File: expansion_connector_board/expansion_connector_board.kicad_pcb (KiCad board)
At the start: 2 copper layers, 139 x 89 mm, 13 parts, among them J1 Conn_01x04, J12 Conn_02x17_Top_Bottom, J13 Conn_01x04, J14 Conn_02x17_Top_Bottom, J2 ESP32 JTAG+UART (TE0790), J3 ESP32 UART Breakout, J4 ESP32 Bootstraps, J5 ESP32 Sensor, J6 ESP32/Peripheral UART Interfa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, U1 ESP32-WROOM-32D

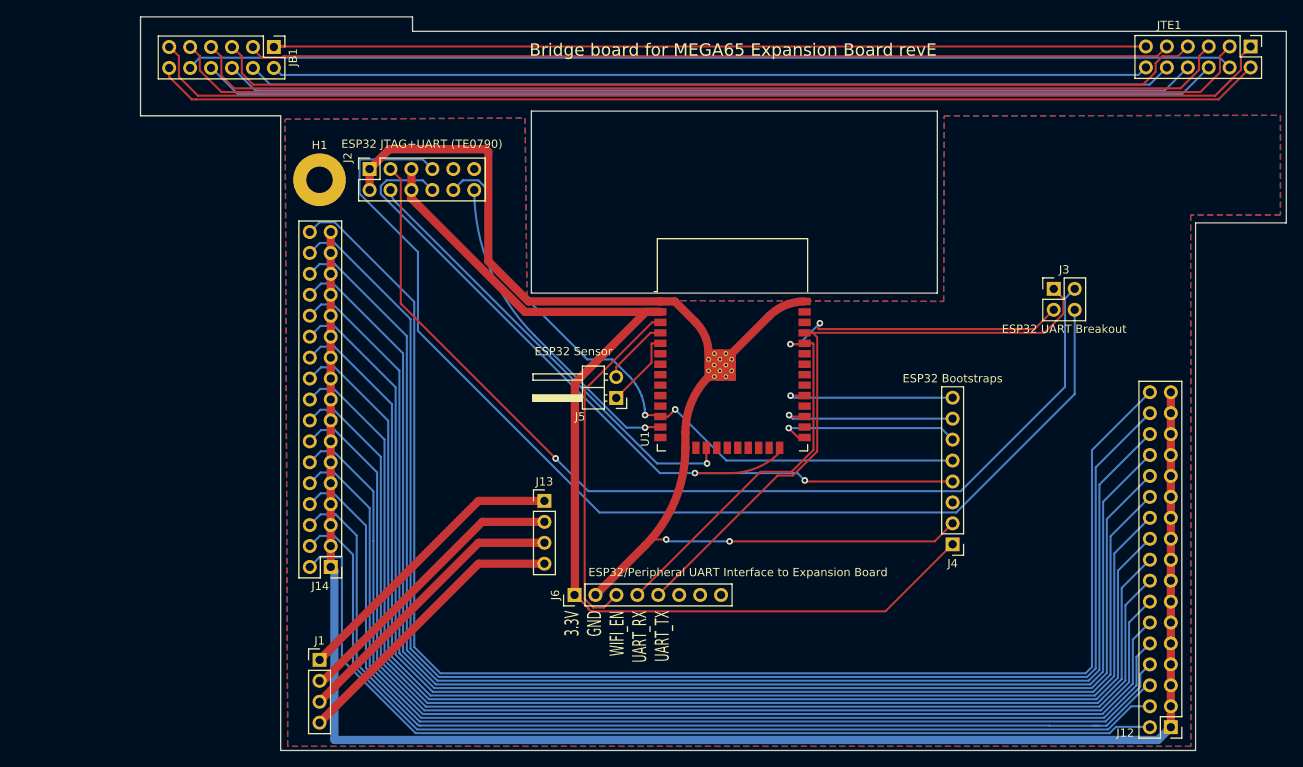
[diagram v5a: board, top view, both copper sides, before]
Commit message: add MEGA65 and open hardware logos etc
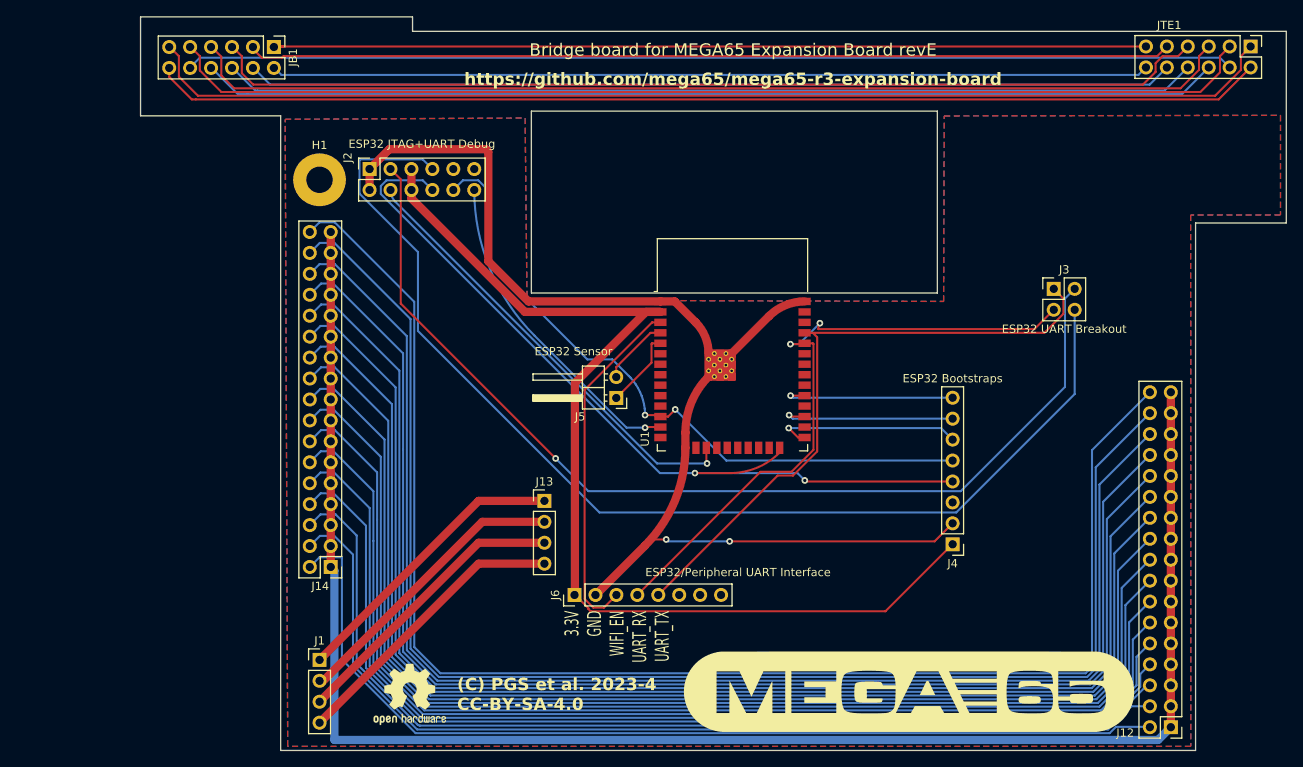
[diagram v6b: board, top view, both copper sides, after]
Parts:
- added G1: LOGO, 00Project:MEGA65-logo, F.Cu at (150.2, 116.9)
- added SYM1: Logo_Open_Hardware_Small, Symbol:OSHW-Logo2_9.8x8mm_SilkScreen, F.Cu at (89.7, 117.2)
- J2: value ESP32 JTAG+UART (TE0790) -> ESP32 JTAG+UART Debug
- J6: value ESP32/Peripheral UART Interface to Expansion Board -> ESP32/Peripheral UART Interface
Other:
- board text added: "(C) PGS et al. 2023-4 CC-BY-SA-4.0"
- board text added: "https://github.com/mega65/mega65-r3-expansion-board"

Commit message: add audio J19 pickup header
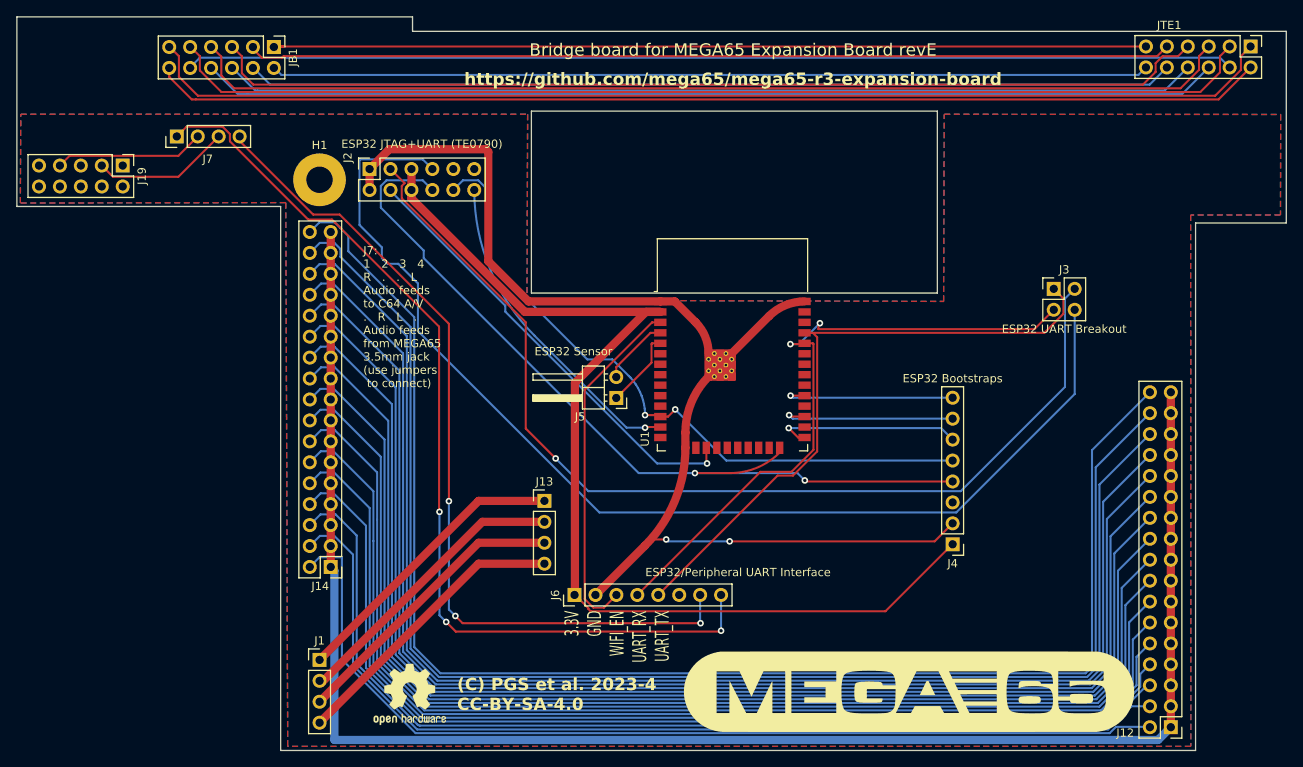
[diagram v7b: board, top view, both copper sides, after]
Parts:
- added J19: MEGA65 R4+ Analog Audio Header, Connector_PinHeader_2.54mm:PinHeader_2x05_P2.54mm_Vertical, F.Cu at (54.8, 53.0)
- added J7: Conn_01x04, Connector_PinHeader_2.54mm:PinHeader_1x04_P2.54mm_Vertical, F.Cu at (61.4, 49.5)
- J2: value ESP32 JTAG+UART Debug -> ESP32 JTAG+UART (TE0790)
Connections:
- J6 pad 7: unconnected-(J6-Pin_7-Pad7) -> AUDIO_L
- J6 pad 8: unconnected-(J6-Pin_8-Pad8) -> AUDIO_R
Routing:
- net AUDIO_R: track 0.00 -> 117.3 mm, vias 0 -> 3
- net AUDIO_L: track 0.00 -> 104.5 mm, vias 0 -> 3
- net Net-(J19-Pin_7): track 0.00 -> 18.2 mm
- net Net-(J19-Pin_3): track 0.00 -> 16.8 mm
- net JTAG_MTDO: track 103.3 -> 104.8 mm
- net /TE0790_B: track 138.0 -> 138.8 mm
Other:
- board size 139 x 89 mm -> 154 x 89 mm
- board text added: "J7: 1 2 3 4 R . . L Audio feeds to C64 A/V . R L . Audio feeds from MEGA65 3.5mm jack (use jumpers to connect)"

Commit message: gerbers exported and uploaded to pcbway
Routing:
- net AUDIO_L: track 104.5 -> 108.1 mm
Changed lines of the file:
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@@
   )
   (dimension (type aligned) (layer "Cmts.User")
-    (pts (xy 57 35) (xy 196.01 35))
+    (pts (xy 42 35) (xy 196.01 35))
     (height -1.913458)
-    (gr_text "139.0100 mm" (at 126.505 31.936542) (layer "Cmts.User")
+    (gr_text "154.0100 mm" (at 119.005 31.936542) (layer "Cmts.User")
       (effects (font (size 1 1) (thickness 0.15)))
     )
@@
   (segment (start 136.1186 81.2038) (end 155.5242 81.2038) (width 0.25) (layer "B.Cu") (net 74))
   (segment (start 135.8646 80.9498) (end 136.1186 81.2038) (width 0.25) (layer "B.Cu") (net 74))
-  (segment (start 69.0218 50.054703) (end 77.945897 58.9788) (width 0.25) (layer "F.Cu") (net 76))
+  (segment (start 70.7546 51.2374) (end 80.174703 51.2374) (width 0.25) (layer "F.Cu") (net 76))
   (segment (start 124.9426 108.5596) (end 96.0766 108.5596) (width 0.25) (layer "F.Cu") (net 76))
+  (segment (start 94.4118 72.2376) (end 94.4118 93.7514) (width 0.25) (layer "F.Cu") (net 76))
+  (segment (start 69.0218 49.5046) (end 70.7546 51.2374) (width 0.25) (layer "F.Cu") (net 76))
   (segment (start 96.0766 108.5596) (end 95.1992 107.6822) (width 0.25) (layer "F.Cu") (net 76))
-  (segment (start 69.0218 49.5046) (end 69.0218 50.054703) (width 0.25) (layer "F.Cu") (net 76))
-  (segment (start 81.153 58.9788) (end 81.9404 59.7662) (width 0.25) (layer "F.Cu") (net 76))
-  (segment (start 81.9404 59.7662) (end 94.4118 72.2376) (width 0.25) (layer "F.Cu") (net 76))
-  (segment (start 94.4118 72.2376) (end 94.4118 93.7514) (width 0.25) (layer "F.Cu") (net 76))
-  (segment (start 77.945897 58.9788) (end 81.153 58.9788) (width 0.25) (layer "F.Cu") (net 76))
+  (segment (start 80.174703 51.2374) (end 82.2396 53.302297) (width 0.25) (layer "F.Cu") (net 76))
+  (segment (start 82.2396 60.0654) (end 94.4118 72.2376) (width 0.25) (layer "F.Cu") (net 76))
+  (segment (start 82.2396 53.302297) (end 82.2396 60.0654) (width 0.25) (layer "F.Cu") (net 76))
   (via (at 124.9426 108.5596) (size 0.8) (drill 0.4) (layers "F.Cu" "B.Cu") (net 76))
   (via (at 94.4118 93.7514) (size 0.8) (drill 0.4) (layers "F.Cu" "B.Cu") (net 76))
@@
   (segment (start 124.8918 105.1306) (end 124.8918 108.5088) (width 0.25) (layer "B.Cu") (net 76))
   (segment (start 94.4118 106.8948) (end 95.1992 107.6822) (width 0.25) (layer "B.Cu") (net 76))
-  (segment (start 67.8468 50.0922) (end 77.343 59.5884) (width 0.25) (layer "F.Cu") (net 77))
   (segment (start 95.25 109.5756) (end 94.0816 108.4072) (width 0.25) (layer "F.Cu") (net 77))
+  (segment (start 61.4018 49.5046) (end 62.5768 48.3296) (width 0.25) (layer "F.Cu") (net 77))
+  (segment (start 70.7247 51.6874) (end 75.1896 56.1523) (width 0.25) (layer "F.Cu") (net 77))
+  (segment (start 93.218 94.996) (end 93.2688 95.0468) (width 0.25) (layer "F.Cu") (net 77))
+  (segment (start 78.555497 59.5884) (end 80.230101 59.5884) (width 0.25) (layer "F.Cu") (net 77))
+  (segment (start 127.3302 109.5756) (end 95.25 109.5756) (width 0.25) (layer "F.Cu") (net 77))
+  (segment (start 66.968501 48.3296) (end 67.8468 49.207899) (width 0.25) (layer "F.Cu") (net 77))
+  (segment (start 127.4318 109.474) (end 127.3302 109.5756) (width 0.25) (layer "F.Cu") (net 77))
+  (segment (start 62.5768 48.3296) (end 66.968501 48.3296) (width 0.25) (layer "F.Cu") (net 77))
+  (segment (start 67.8468 49.207899) (end 67.8468 49.991301) (width 0.25) (layer "F.Cu") (net 77))
   (segment (start 93.218 72.576299) (end 93.218 94.996) (width 0.25) (layer "F.Cu") (net 77))
-  (segment (start 62.5768 48.3296) (end 66.968501 48.3296) (width 0.25) (layer "F.Cu") (net 77))
+  (segment (start 75.1896 56.1523) (end 75.1896 56.222503) (width 0.25) (layer "F.Cu") (net 77))
+  (segment (start 69.542899 51.6874) (end 70.7247 51.6874) (width 0.25) (layer "F.Cu") (net 77))
   (segment (start 80.230101 59.5884) (end 93.218 72.576299) (width 0.25) (layer "F.Cu") (net 77))
-  (segment (start 127.3302 109.5756) (end 95.25 109.5756) (width 0.25) (layer "F.Cu") (net 77))
-  (segment (start 127.4318 109.474) (end 127.3302 109.5756) (width 0.25) (layer "F.Cu") (net 77))
-  (segment (start 66.968501 48.3296) (end 67.8468 49.207899) (width 0.25) (layer "F.Cu") (net 77))
-  (segment (start 77.343 59.5884) (end 80.230101 59.5884) (width 0.25) (layer "F.Cu") (net 77))
-  (segment (start 61.4018 49.5046) (end 62.5768 48.3296) (width 0.25) (layer "F.Cu") (net 77))
-  (segment (start 93.218 94.996) (end 93.2688 95.0468) (width 0.25) (layer "F.Cu") (net 77))
-  (segment (start 67.8468 49.207899) (end 67.8468 50.0922) (width 0.25) (layer "F.Cu") (net 77))
+  (segment (start 75.1896 56.222503) (end 78.555497 59.5884) (width 0.25) (layer "F.Cu") (net 77))
+  (segment (start 67.8468 49.991301) (end 69.542899 51.6874) (width 0.25) (layer "F.Cu") (net 77))
   (via (at 127.4318 109.474) (size 0.8) (drill 0.4) (layers "F.Cu" "B.Cu") (net 77))
   (via (at 94.0816 108.4072) (size 0.8) (drill 0.4) (layers "F.Cu" "B.Cu") (net 77))
